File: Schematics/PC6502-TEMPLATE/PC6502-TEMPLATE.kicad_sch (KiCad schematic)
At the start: 7 parts, among them J1 BUS

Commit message: Add Power/Storage PCB
Also tidied template
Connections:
- net SPCLK renamed CPU_CLK
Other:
- note added: "I now realise that some peripherals need the stretched CPU clock, DOH! So I'll mod wire the CPU_CLOCK on the main CPU board to SP_CLK :("
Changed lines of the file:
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@@
+		)
+	)
+	(text "I now realise that some peripherals \nneed the stretched CPU clock, DOH!\nSo I'll mod wire the CPU_CLOCK on \nthe main CPU board to SP_CLK :("
+		(exclude_from_sim no)
+		(at 252.222 145.288 0)
+		(effects
+			(font
+				(size 1.27 1.27)
+			)
 		)
 	)
@@
 	)
 	(junction
+		(at 233.68 124.46)
+		(diameter 0)
+		(color 0 0 0 0)
+	)
+	(junction
 		(at 227.33 66.04)
 		(diameter 0)
@@
 		)
 	)
+	(wire
+		(pts
+			(xy 233.68 138.43) (xy 233.68 124.46)
+		)
+		(stroke
+			(width 0)
+			(type default)
+		)
+	)
 	(bus
 		(pts
@@
 	(wire
 		(pts
-			(xy 223.52 124.46) (xy 236.22 124.46)
+			(xy 223.52 124.46) (xy 233.68 124.46)
 		)
 		(stroke
@@
 	(wire
 		(pts
+			(xy 242.57 138.43) (xy 233.68 138.43)
+		)
+		(stroke
+			(width 0)
+			(type default)
+		)
+	)
+	(wire
+		(pts
 			(xy 227.33 58.42) (xy 227.33 60.96)
 		)
@@
 		(pts
 			(xy 196.85 60.96) (xy 196.85 63.5)
+		)
+		(stroke
+			(width 0)
+			(type default)
+		)
+	)
+	(wire
+		(pts
+			(xy 233.68 124.46) (xy 236.22 124.46)
 		)
 		(stroke
@@
 				(hide yes)
 			)
+		)
+	)
+	(global_label "CPU_CLK"
+		(shape output)
+		(at 242.57 138.43 0)
+		(fields_autoplaced yes)
+		(effects
+			(font
+				(size 1.27 1.27)
+			)
+			(justify left)
+		)
+		(property "Intersheetrefs" "${INTERSHEET_REFS}"
+			(at 253.9614 138.43 0)
+			(effects
+				(font
+					(size 1.27 1.27)
+				)
+				(justify left)
+				(hide yes)
+			)

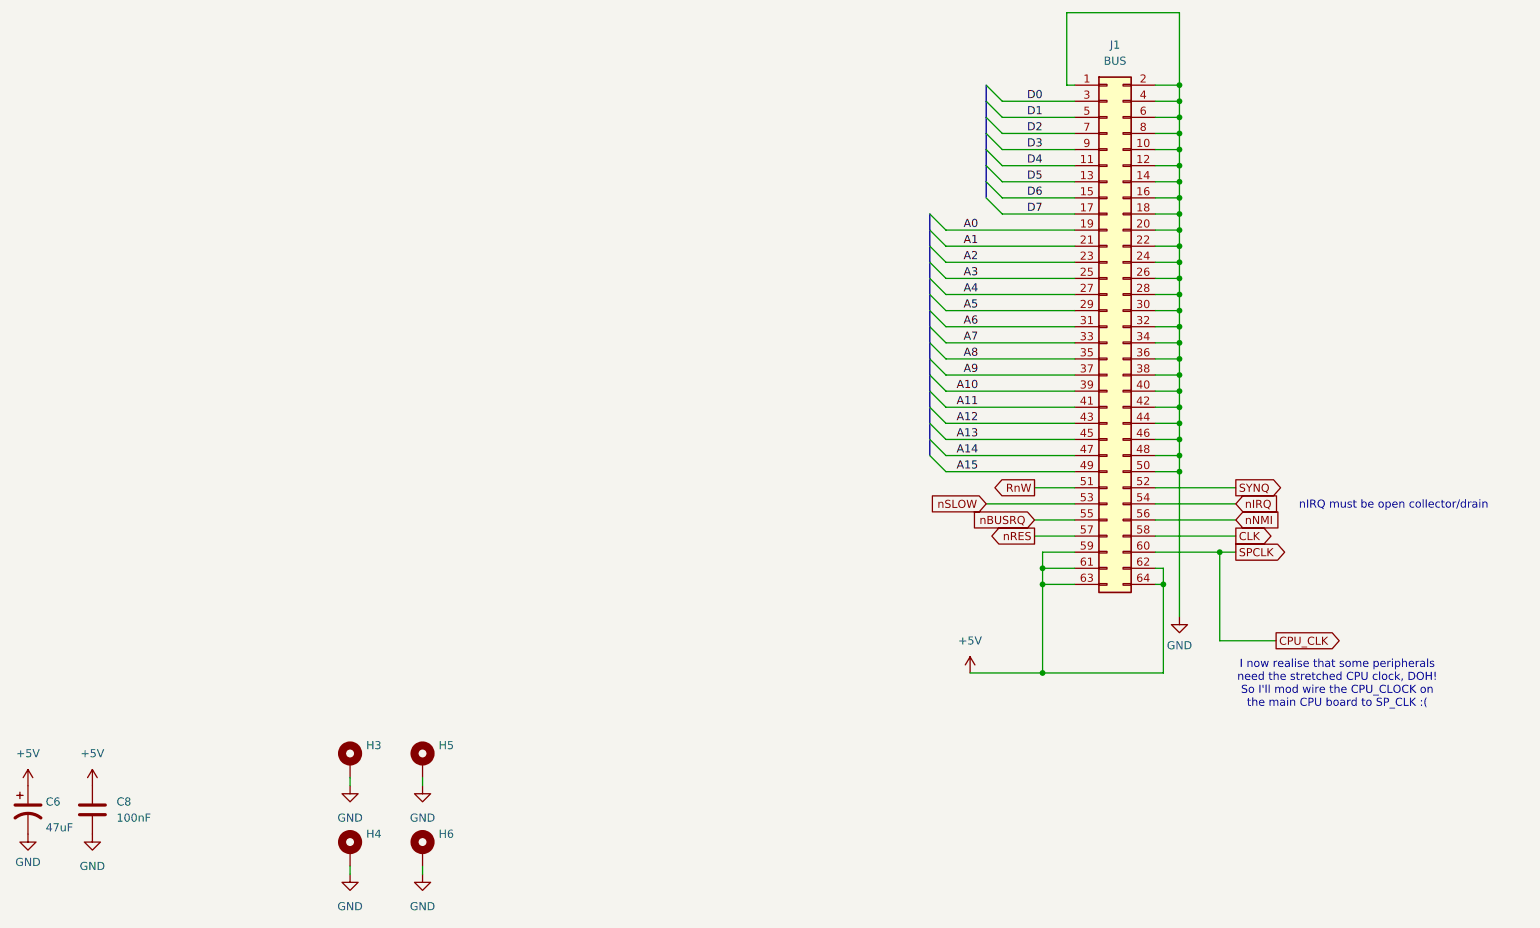
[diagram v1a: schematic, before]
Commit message: V1.1 CPU, VIA and POWER PCBs uploaded
A simpler CPU board (direct link to FT245R, 74161 removed and some tidying of tracks). Fixed a couple of floating inputs to RAM/ROM
VIA is much simpler, having just the one VIA chip.
POWER board has USB-PD and a 24VDC input for higher power stuff in the future.
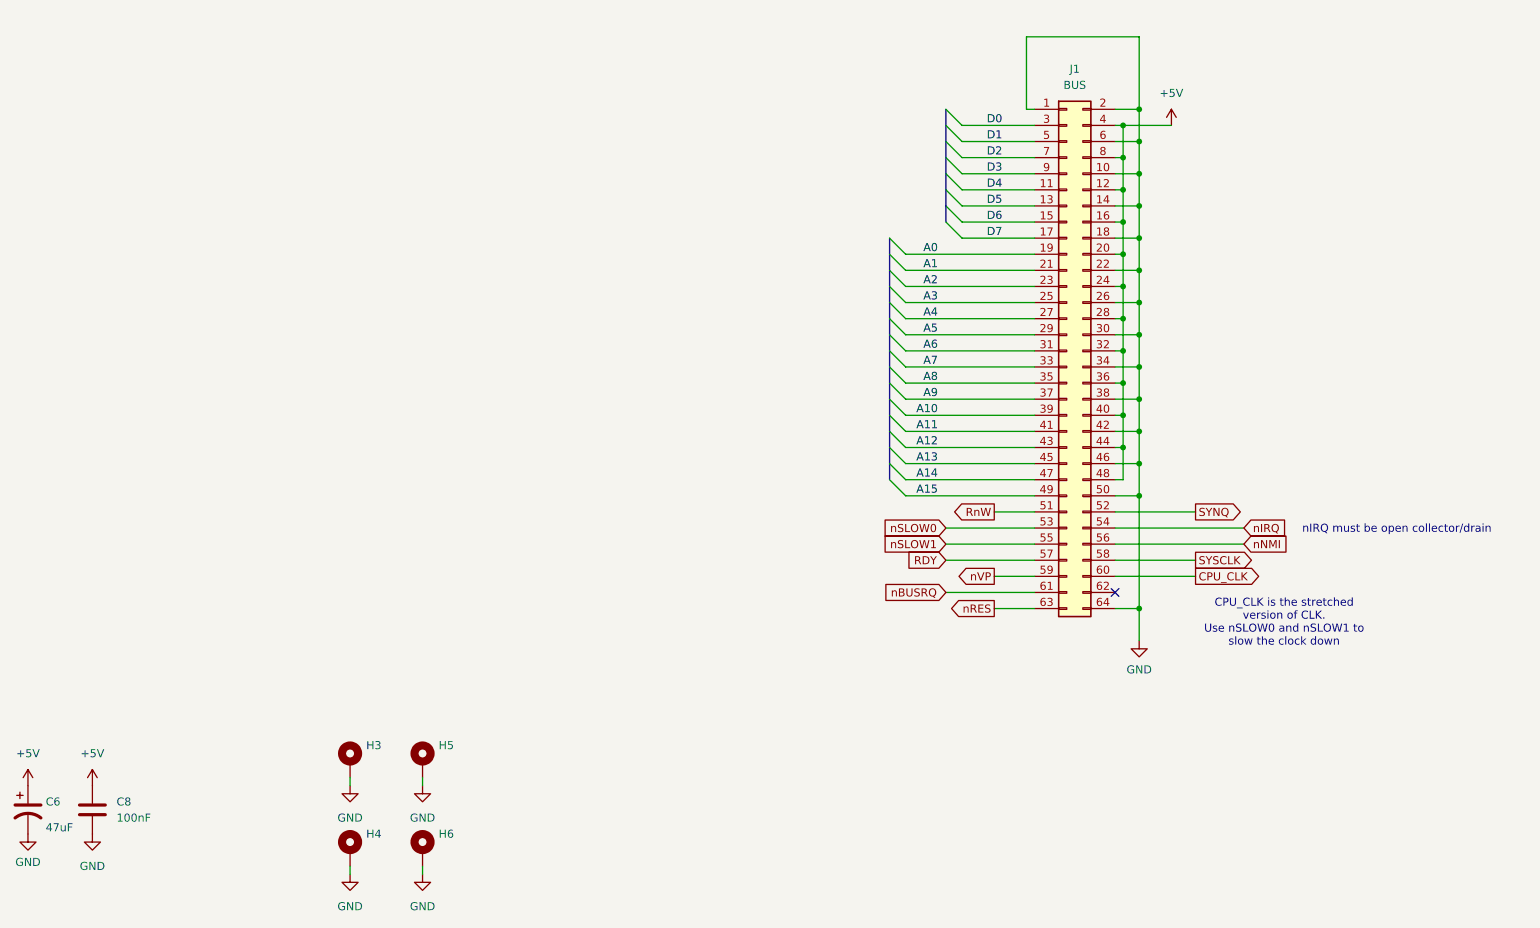
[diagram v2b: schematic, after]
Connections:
- net +5V: now also J1.12 (Pin_12), J1.16 (Pin_16), J1.20 (Pin_20), J1.24 (Pin_24), J1.28 (Pin_28), J1.32 (Pin_32), J1.36 (Pin_36), J1.4 (Pin_4), J1.40 (Pin_40), J1.44 (Pin_44), J1.48 (Pin_48), J1.8 (Pin_8); no longer J1.59 (Pin_59), J1.61 (Pin_61), J1.62 (Pin_62), J1.63 (Pin_63), J1.64 (Pin_64)
- net GND: now also J1.64 (Pin_64); no longer J1.12 (Pin_12), J1.16 (Pin_16), J1.20 (Pin_20), J1.24 (Pin_24), J1.28 (Pin_28), J1.32 (Pin_32), J1.36 (Pin_36), J1.4 (Pin_4), J1.40 (Pin_40), J1.44 (Pin_44), J1.48 (Pin_48), J1.8 (Pin_8)
- net nBUSRQ: now also J1.61 (Pin_61); no longer J1.55 (Pin_55)
- net nRES: now also J1.63 (Pin_63); no longer J1.57 (Pin_57)
- net CLK renamed SYSCLK
- net nSLOW renamed nSLOW0
- new net RDY: J1.57 (Pin_57)
- new net nSLOW1: J1.55 (Pin_55)
- new net nVP: J1.59 (Pin_59)
- no-connect marks 0 -> 1
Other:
- note added: "CPU_CLK is the stretched version of CLK. Use nSLOW0 and nSLOW1 to slow the clock down"
- note removed: "I now realise that some peripherals need the stretched CPU clock, DOH! So I'll mod wire the CPU_CLOCK on the main CPU board to SP_CLK :("
- moved on the sheet: J1
